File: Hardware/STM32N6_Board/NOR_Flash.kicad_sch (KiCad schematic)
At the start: 16 parts, among them U7 MX25LM51245GXDI00, U8 SPX5205-ADJ

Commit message: Completed schematic layout, ERC check, and footprint assignment
- Completed and checked the schematic layout
- Ran the ERC check; no errors (but lots of (checked) warnings)
- Assigned footprints. Most in std lib, others in footprints.pretty
- Imported the components to the PCB Editor, and fixed errors
- All that's left is PCB layout!
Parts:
- C43, C44, C45, C46, C47, C48, C50: footprint (none) -> Capacitor_SMD:C_0805_2012Metric_Pad1.18x1.45mm_HandSolder
- D12: footprint (none) -> LED_SMD:LED_0805_2012Metric_Pad1.15x1.40mm_HandSolder
- R13, R14, R16, R17, R21, R22: footprint (none) -> Resistor_SMD:R_0805_2012Metric_Pad1.20x1.40mm_HandSolder
- U7: footprint (none) -> STM32N6_Footprints:MX25LM51245GXD100_BGA24C100P5X5_600X800X120
- U8: footprint (none) -> Package_TO_SOT_SMD:SOT-23-5
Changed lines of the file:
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@@
 			)
 		)
-		(property "Footprint" ""
+		(property "Footprint" "Resistor_SMD:R_0805_2012Metric_Pad1.20x1.40mm_HandSolder"
 			(at 58.42 58.42 0)
 			(effects
@@
 			)
 		)
-		(property "Footprint" ""
+		(property "Footprint" "STM32N6_Footprints:MX25LM51245GXD100_BGA24C100P5X5_600X800X120"
 			(at 77.47 40.64 0)
 			(effects
@@
 			)
 		)
-		(property "Footprint" ""
+		(property "Footprint" "Capacitor_SMD:C_0805_2012Metric_Pad1.18x1.45mm_HandSolder"
 			(at 109.22 36.83 0)
 			(effects
@@
 			)
 		)
-		(property "Footprint" ""
+		(property "Footprint" "Capacitor_SMD:C_0805_2012Metric_Pad1.18x1.45mm_HandSolder"
 			(at 144.78 36.83 0)
 			(effects
@@
 			)
 		)
-		(property "Footprint" ""
+		(property "Footprint" "Resistor_SMD:R_0805_2012Metric_Pad1.20x1.40mm_HandSolder"
 			(at 118.11 114.3 0)
 			(effects
@@
 			)
 		)
-		(property "Footprint" ""
+		(property "Footprint" "Capacitor_SMD:C_0805_2012Metric_Pad1.18x1.45mm_HandSolder"
 			(at 118.11 36.83 0)
 			(effects
@@
 			)
 		)
-		(property "Footprint" ""
+		(property "Footprint" "Capacitor_SMD:C_0805_2012Metric_Pad1.18x1.45mm_HandSolder"
 			(at 100.33 36.83 0)
 			(effects
@@
 			)
 		)
-		(property "Footprint" ""
+		(property "Footprint" "Capacitor_SMD:C_0805_2012Metric_Pad1.18x1.45mm_HandSolder"
 			(at 127 36.83 0)
 			(effects
@@
 			)
 		)
-		(property "Footprint" ""
+		(property "Footprint" "Resistor_SMD:R_0805_2012Metric_Pad1.20x1.40mm_HandSolder"
 			(at 77.47 121.92 0)
 			(effects
@@
 			)
 		)
-		(property "Footprint" ""
+		(property "Footprint" "Package_TO_SOT_SMD:SOT-23-5"
 			(at 93.98 166.37 0)
 			(effects
@@
 			)
 		)
-		(property "Footprint" ""
+		(property "Footprint" "Capacitor_SMD:C_0805_2012Metric_Pad1.18x1.45mm_HandSolder"
 			(at 116.84 172.72 0)
 			(effects
@@
 			)
 		)
-		(property "Footprint" ""
+		(property "Footprint" "Resistor_SMD:R_0805_2012Metric_Pad1.20x1.40mm_HandSolder"
 			(at 107.95 168.91 0)
 			(effects
@@
 			)
 		)
-		(property "Footprint" ""
+		(property "Footprint" "Capacitor_SMD:C_0805_2012Metric_Pad1.18x1.45mm_HandSolder"
 			(at 135.89 36.83 0)
 			(effects
@@
 			)
 		)
-		(property "Footprint" ""
+		(property "Footprint" "Resistor_SMD:R_0805_2012Metric_Pad1.20x1.40mm_HandSolder"
 			(at 107.95 176.53 0)
 			(effects
@@
 			)
 		)
-		(property "Footprint" ""
+		(property "Footprint" "Resistor_SMD:R_0805_2012Metric_Pad1.20x1.40mm_HandSolder"
 			(at 77.47 110.49 0)
 			(effects
@@
 			)
 		)
-		(property "Footprint" ""
+		(property "Footprint" "LED_SMD:LED_0805_2012Metric_Pad1.15x1.40mm_HandSolder"
 			(at 127 172.72 0)
 			(effects

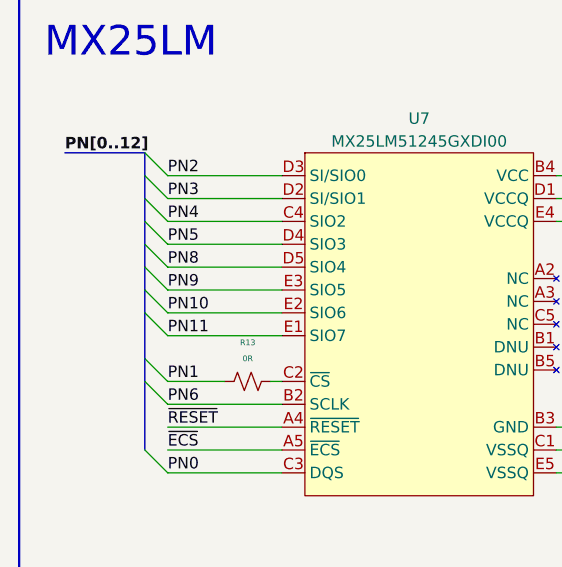
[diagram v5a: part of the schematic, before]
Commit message: Completed a lot of the layout of the STM Board
- Major layout complete, but all the wiring still left. 488 open nets!
- The STM32's BGA fanout is complete, now comes laying out traces
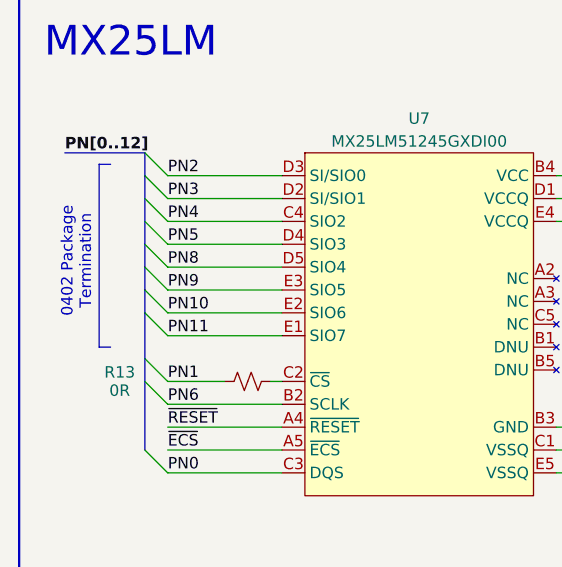
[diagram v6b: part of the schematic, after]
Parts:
- C43, C44, C45, C46, C47, C48: footprint Capacitor_SMD:C_0805_2012Metric_Pad1.18x1.45mm_HandSolder -> Capacitor_SMD:C_0402_1005Metric
- R13, R14, R16, R17: footprint Resistor_SMD:R_0805_2012Metric_Pad1.20x1.40mm_HandSolder -> Resistor_SMD:R_0402_1005Metric
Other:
- note added: "0402 Package Termination"
